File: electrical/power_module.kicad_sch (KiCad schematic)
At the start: 15 parts, among them J1 Screw_Terminal_01x01, J2 Screw_Terminal_01x01, J3 Ground connector from bulb wi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, Q1 IRF5305, Q2 BC547

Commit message: Fixes in power module
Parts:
- removed D2: 1N4001, Diode_THT:D_DO-41_SOD81_P10.16mm_Horizontal, symbol Diode:1N4001
- added C5: ?, symbol Device:C
- J1, J2: value Screw_Terminal_01x01 -> Need to cut positive bulb wiring
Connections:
- net VDC is gone; now on an unnamed net: R2.1
- net BULB STATUS: now also R6.1; no longer R6.2
- net GND: now also B1.1 (-), C5.2; no longer Q1.2 (D)
- net at F1.2, J1.1 (Pin_1): now also Q1.3 (S); no longer B1.2 (+)
- new net: B1.2 (+), C5.1, J2.1 (Pin_1), Q1.2 (D), R1.1, R6.2
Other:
- note removed: "Need to cut negative bulb wiring"
- moved on the sheet: B1, D1, F1, J1, J2, J3, R1, R6

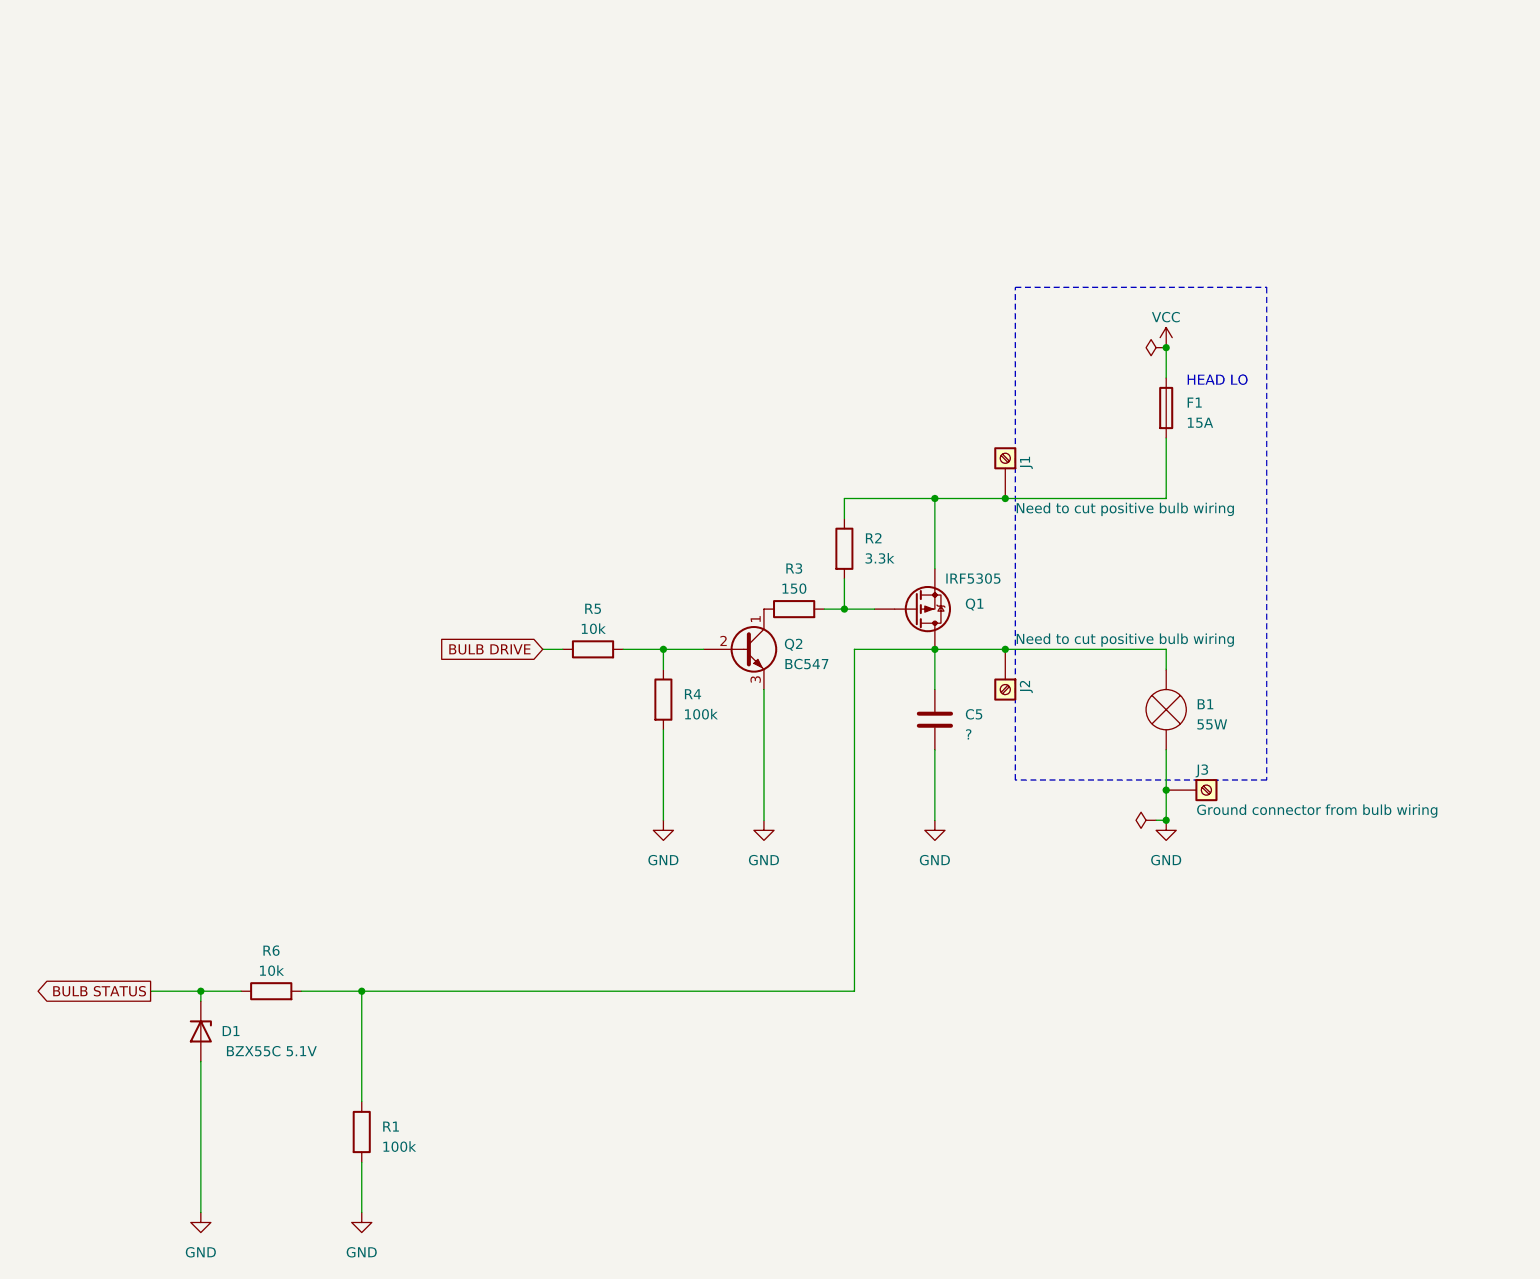
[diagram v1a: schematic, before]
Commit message: Added power module with MOSFET-N
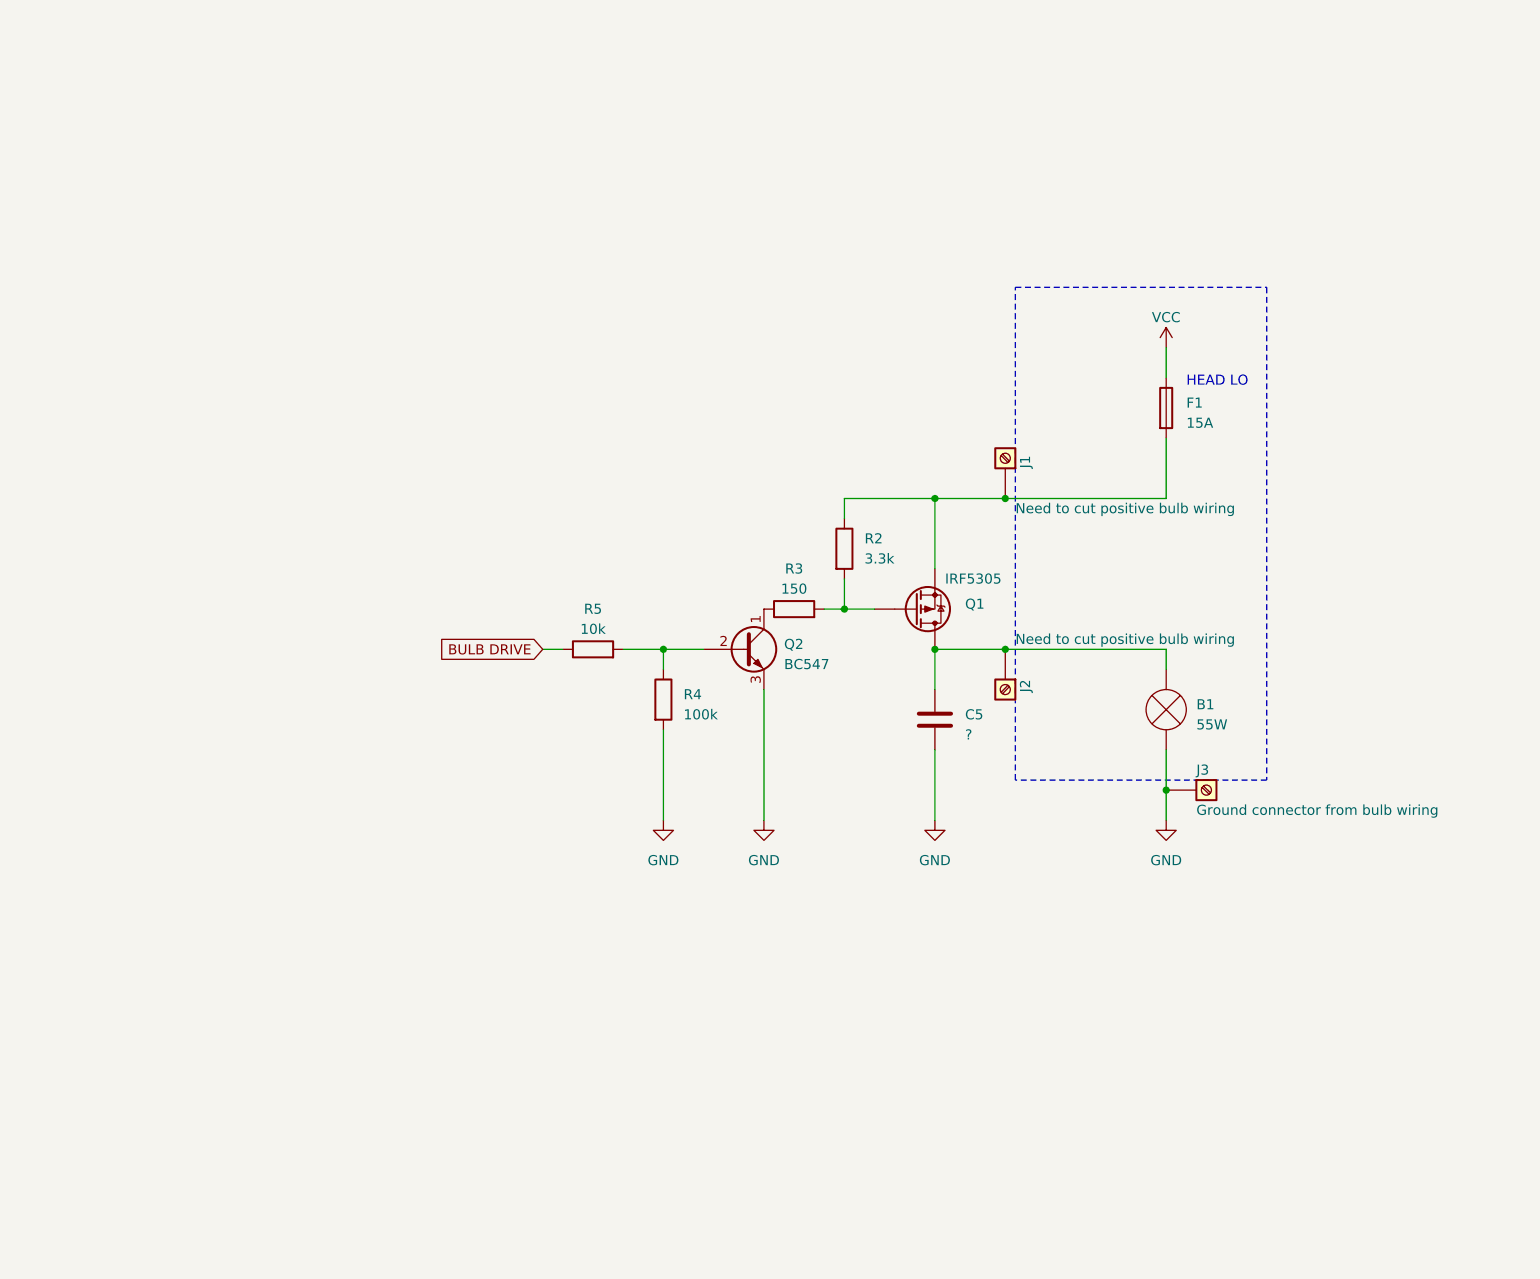
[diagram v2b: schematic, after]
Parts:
- removed D1: BZX55C 5.1V, Diode_THT:D_DO-35_SOD27_P7.62mm_Horizontal, symbol Diode:BZX84Cxx
- removed R1: 100k, symbol Device:R
- removed R6: 10k, symbol Device:R
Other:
- title: Power module -> Power module P

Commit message: Updated according to recent changes
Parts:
- added D8: 1N4002, Diode_THT:D_DO-41_SOD81_P10.16mm_Horizontal, symbol Diode:1N4002
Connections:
- net at F1.2, J1.1 (Pin_1), Q1.3 (S)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: now also D8.2 (A)
- net BULB DRIVE renamed BEAM_IN
- new net POWER_12: D8.1 (K)
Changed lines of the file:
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@@
+    (stroke (width 0) (type default))
+  )
+  (wire (pts (xy 173.99 76.2) (xy 173.99 66.04))
     (stroke (width 0) (type default))
   )
@@
     (stroke (width 0) (type default))
   )
+  (wire (pts (xy 173.99 66.04) (xy 161.29 66.04))
+    (stroke (width 0) (type default))
+  )
   (wire (pts (xy 139.7 110.49) (xy 139.7 113.03))
     (stroke (width 0) (type default))
   )
   (wire (pts (xy 134.62 110.49) (xy 139.7 110.49))
+    (stroke (width 0) (type default))
+  )
+  (wire (pts (xy 173.99 83.82) (xy 173.99 91.44))
     (stroke (width 0) (type default))
   )
@@
     (effects (font (size 1.27 1.27)) (justify left bottom))
   )
-  (global_label "BULB DRIVE" (shape input) (at 124.46 110.49 180) (fields_autoplaced)
+  (global_label "POWER_12" (shape bidirectional) (at 161.29 66.04 180) (fields_autoplaced)
     (effects (font (size 1.27 1.27)) (justify right))
-    (property "Intersheetrefs" "${INTERSHEET_REFS}" (at 110.3056 110.49 0)
+    (property "Intersheetrefs" "${INTERSHEET_REFS}" (at 147.4154 66.04 0)
+      (effects (font (size 1.27 1.27)) (justify right) hide)
+    )
+  )
+  (global_label "BEAM_IN" (shape input) (at 124.46 110.49 180) (fields_autoplaced)
+    (effects (font (size 1.27 1.27)) (justify right))
+    (property "Intersheetrefs" "${INTERSHEET_REFS}" (at 113.6923 110.49 0)
       (effects (font (size 1.27 1.27)) (justify right) hide)
     )
@@
         )
       )
+    )
+  )
+  (symbol (lib_id "Diode:1N4002") (at 173.99 80.01 270) (unit 1)
+    (in_bom yes) (on_board yes) (dnp no) (fields_autoplaced)
+    (property "Reference" "D8" (at 176.53 79.375 90)
+      (effects (font (size 1.27 1.27)) (justify left))
+    )
+    (property "Value" "1N4002" (at 176.53 81.915 90)
+      (effects (font (size 1.27 1.27)) (justify left))
+    )
+    (property "Footprint" "Diode_THT:D_DO-41_SOD81_P10.16mm_Horizontal" (at 169.545 80.01 0)
+      (effects (font (size 1.27 1.27)) hide)
+    )
+    (property "Datasheet" "http://www.vishay.com/docs/88503/1n4001.pdf" (at 173.99 80.01 0)
+      (effects (font (size 1.27 1.27)) hide)
+    )
+    (property "Sim.Device" "D" (at 173.99 80.01 0)
+      (effects (font (size 1.27 1.27)) hide)
+    )
+    (property "Sim.Pins" "1=K 2=A" (at 173.99 80.01 0)
+      (effects (font (size 1.27 1.27)) hide)
+    )
+    (pin "1")
+    (pin "2")
+    (instances
+      (project "led_drive"
+        (path "/01e69042-7c7e-48e9-b7c3-459316fd17f1/8dbccfbf-0961-4856-9879-280cfe95837a"
+          (reference "D8") (unit 1)
+        )
+        (path "/01e69042-7c7e-48e9-b7c3-459316fd17f1/bc381f99-814a-407f-b047-30e2660febd1"
+          (reference "D11") (unit 1)
+        )
+      )

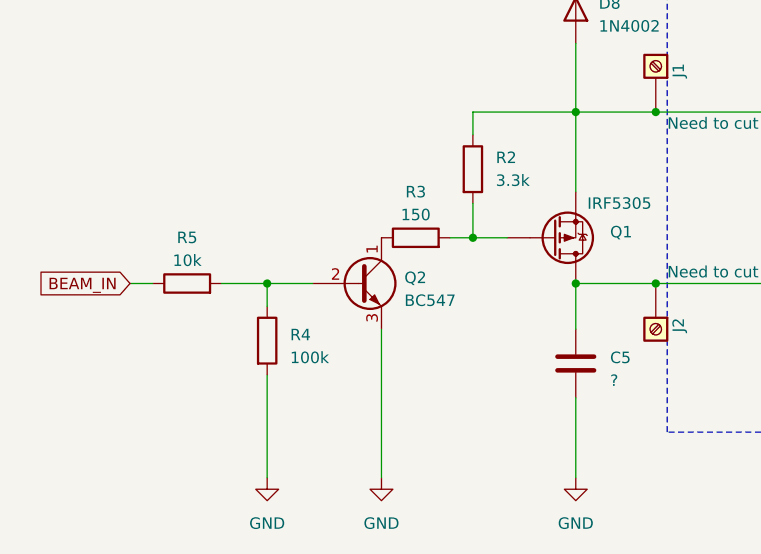
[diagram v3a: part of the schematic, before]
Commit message: Electrical diagram refactor
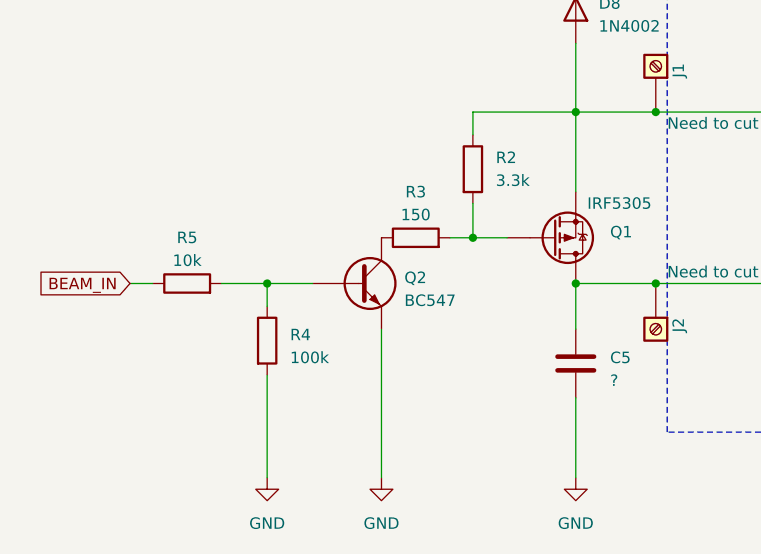
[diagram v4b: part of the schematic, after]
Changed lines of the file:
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@@
         )
         (path "/01e69042-7c7e-48e9-b7c3-459316fd17f1/bc381f99-814a-407f-b047-30e2660febd1"
-          (reference "J2") (unit 1)
+          (reference "J1") (unit 1)
         )
       )
@@
         )
         (path "/01e69042-7c7e-48e9-b7c3-459316fd17f1/bc381f99-814a-407f-b047-30e2660febd1"
-          (reference "J1") (unit 1)
+          (reference "J2") (unit 1)
         )
       )
@@
         )
         (path "/01e69042-7c7e-48e9-b7c3-459316fd17f1/bc381f99-814a-407f-b047-30e2660febd1"
-          (reference "F2") (unit 1)
-        )
-      )
+          (reference "F6") (unit 1)
+        )
+      )

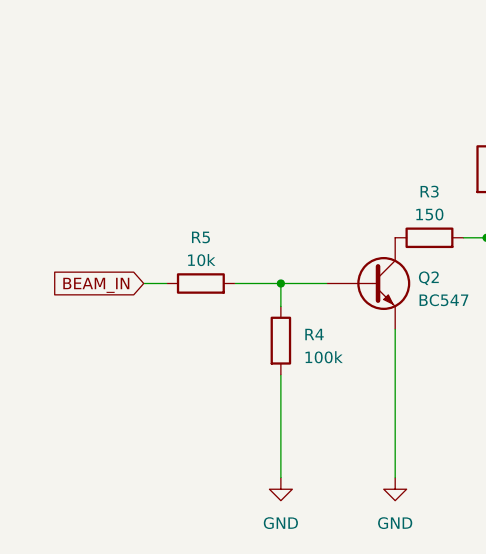
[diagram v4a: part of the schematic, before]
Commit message: What a terrible mistake - fixed BEAM IN/OUT
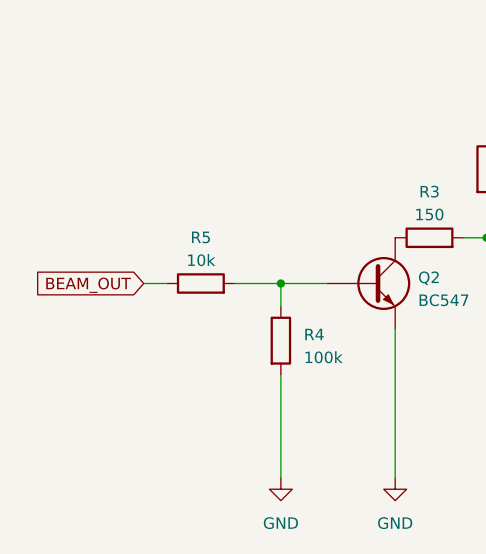
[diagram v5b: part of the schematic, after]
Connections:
- net BEAM_IN renamed BEAM_OUT
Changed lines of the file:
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@@
     )
   )
-  (global_label "BEAM_IN" (shape input) (at 124.46 110.49 180) (fields_autoplaced)
+  (global_label "BEAM_OUT" (shape input) (at 124.46 110.49 180) (fields_autoplaced)
     (effects (font (size 1.27 1.27)) (justify right))
-    (property "Intersheetrefs" "${INTERSHEET_REFS}" (at 113.6923 110.49 0)
+    (property "Intersheetrefs" "${INTERSHEET_REFS}" (at 111.999 110.49 0)
       (effects (font (size 1.27 1.27)) (justify right) hide)
     )
